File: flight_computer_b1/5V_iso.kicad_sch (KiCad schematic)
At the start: 1 part, among them U7 MIC94161YCS-TR

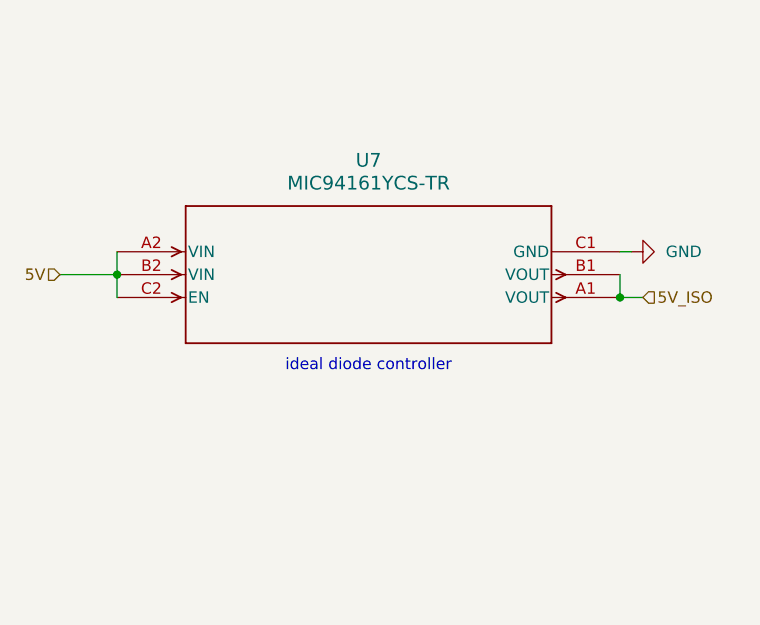
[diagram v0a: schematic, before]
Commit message: flight computer: added mux and voltage sense channels
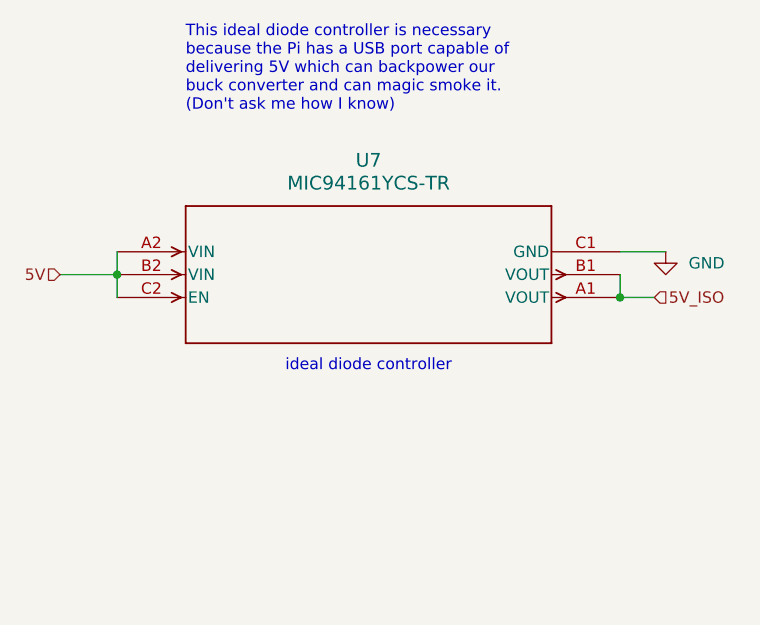
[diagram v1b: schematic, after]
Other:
- note added: "This ideal diode controller is necessary because the Pi has a USB port capable of delivering 5V which can backpower our buck converter and can magic smoke it. (Don't ask me how I know)"
- company: (none) -> Purdue Space Program Liquids
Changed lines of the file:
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@@
 	(generator_version "9.0")
 	(paper "A4")
+	(title_block
+		(date "2025-11-05")
+		(rev "1")
+		(company "Purdue Space Program Liquids")
+	)
 	(text "ideal diode controller"
 		(exclude_from_sim no)
@@
 				(size 1.27 1.27)
 			)
+		)
+	)
+	(text "This ideal diode controller is necessary\nbecause the Pi has a USB port capable of\ndelivering 5V which can backpower our\nbuck converter and can magic smoke it.\n(Don't ask me how I know)"
+		(exclude_from_sim no)
+		(at 114.3 69.85 0)
+		(effects
+			(font
+				(size 1.27 1.27)
+			)
+			(justify left)
 		)
 	)
@@
 	(wire
 		(pts
-			(xy 162.56 95.25) (xy 165.1 95.25)
+			(xy 162.56 95.25) (xy 166.37 95.25)
 		)
 		(stroke
@@
 	(wire
 		(pts
-			(xy 163.83 90.17) (xy 162.56 90.17)
+			(xy 167.64 90.17) (xy 162.56 90.17)
 		)
 		(stroke
@@
 	(hierarchical_label "5V_ISO"
 		(shape input)
-		(at 165.1 95.25 0)
+		(at 166.37 95.25 0)
 		(effects
 			(font
@@
 	(symbol
 		(lib_id "power:GND")
-		(at 163.83 90.17 90)
+		(at 167.64 90.17 0)
 		(unit 1)
 		(exclude_from_sim no)
@@
 		(fields_autoplaced yes)
 		(property "Reference" "#PWR055"
-			(at 170.18 90.17 0)
+			(at 167.64 96.52 0)
 			(effects
 				(font
@@
 		)
 		(property "Value" "GND"
-			(at 167.64 90.1699 90)
+			(at 170.18 91.4399 0)
 			(effects
 				(font
 					(size 1.27 1.27)
 				)
-				(justify right)
+				(justify left)
 			)
 		)
 		(property "Footprint" ""
-			(at 163.83 90.17 0)
+			(at 167.64 90.17 0)
 			(effects
 				(font
@@
 		)
 		(property "Datasheet" ""
-			(at 163.83 90.17 0)
+			(at 167.64 90.17 0)
 			(effects
 				(font
@@
 		)
 		(property "Description" "Power symbol creates a global label with name \"GND\" , ground"
-			(at 163.83 90.17 0)
+			(at 167.64 90.17 0)
 			(effects
 				(font

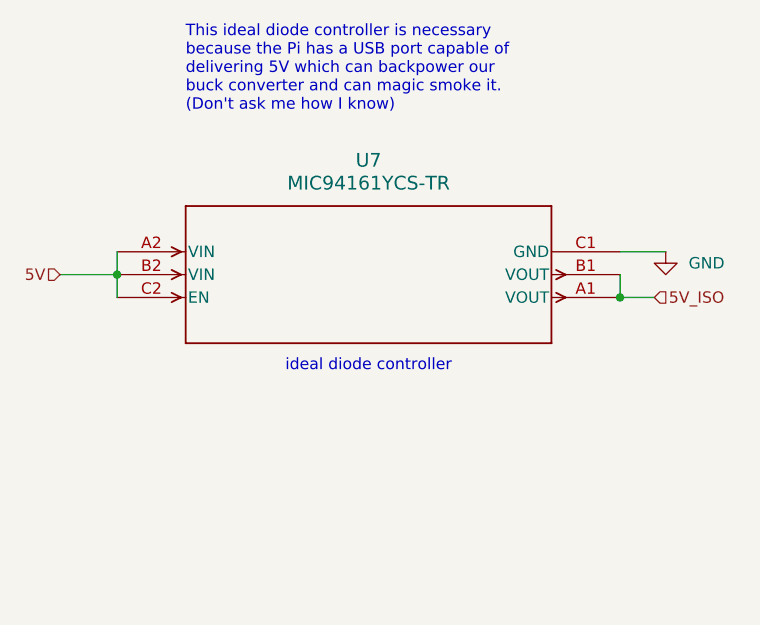
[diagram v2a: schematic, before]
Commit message: flight computer: new ideal diode, small schematic changes
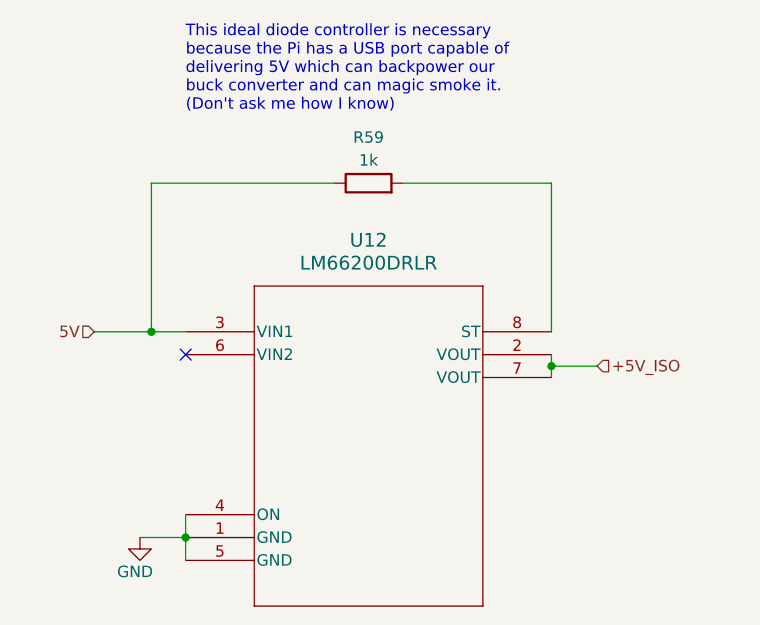
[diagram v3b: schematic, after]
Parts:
- removed U7: MIC94161YCS-TR, avi_lib:MIC94161YCS_TR, symbol avi_lib:MIC94161YCS-TR
- added R59: 1k, Resistor_SMD:R_0603_1608Metric, symbol Device:R
- added U12: LM66200DRLR, avi_lib:SOT-5X3_DRL_TEX-L, symbol avi_lib:LM66200DRLR
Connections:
- net 5V: now also R59.1, U12.3 (VIN1)
- net GND: now also U12.1 (GND), U12.4 (ON), U12.5 (GND)
- new net: R59.2, U12.8 (ST)
- new net +5V_ISO: U12.2 (VOUT), U12.7 (VOUT)
- no-connect marks 0 -> 1
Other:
- note removed: "ideal diode controller"

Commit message: flight computer: routing updates
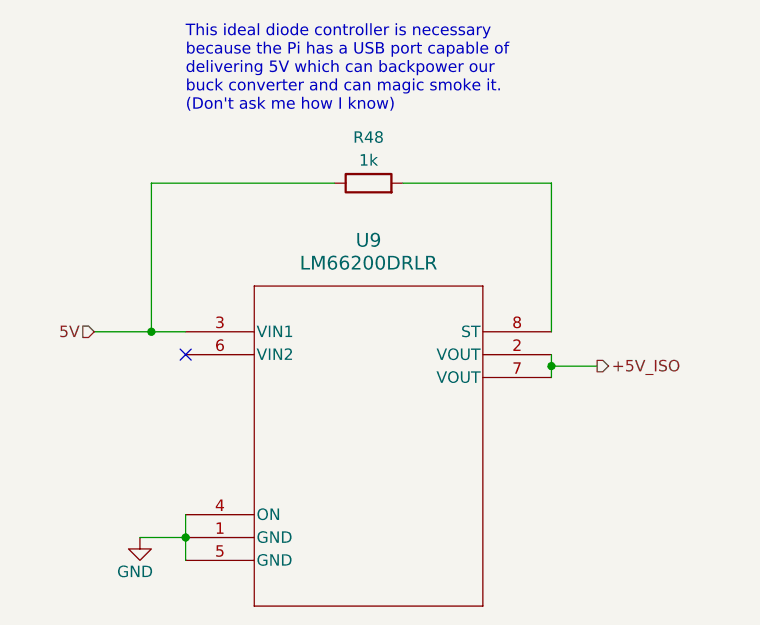
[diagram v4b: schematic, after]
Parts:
- renumbered R59 to R48, U12 to U9
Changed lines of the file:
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@@
 	)
 	(hierarchical_label "+5V_ISO"
-		(shape input)
+		(shape output)
 		(at 160.02 102.87 0)
 		(effects
@@
 		(on_board yes)
 		(dnp no)
-		(property "Reference" "#PWR055"
+		(property "Reference" "#PWR062"
 			(at 109.22 128.27 0)
 			(effects
@@
 			(project "flight_computer"
 				(path "/b71a7b79-cdb5-4e38-a72c-0daaa3474f05/4c75cebc-ee68-4292-a47b-c723457cf341"
-					(reference "#PWR055")
+					(reference "#PWR062")
 					(unit 1)
 				)
@@
 		(on_board yes)
 		(dnp no)
-		(property "Reference" "R59"
+		(property "Reference" "R48"
 			(at 134.62 77.47 90)
 			(effects
@@
 			(project "flight_computer"
 				(path "/b71a7b79-cdb5-4e38-a72c-0daaa3474f05/4c75cebc-ee68-4292-a47b-c723457cf341"
-					(reference "R59")
+					(reference "R48")
 					(unit 1)
 				)
@@
 		(dnp no)
 		(fields_autoplaced yes)
-		(property "Reference" "U12"
+		(property "Reference" "U9"
 			(at 134.62 88.9 0)
 			(effects
@@
 			(project ""
 				(path "/b71a7b79-cdb5-4e38-a72c-0daaa3474f05/4c75cebc-ee68-4292-a47b-c723457cf341"
-					(reference "U12")
+					(reference "U9")
 					(unit 1)
 				)

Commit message: flight computer: new pyro circuit
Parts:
- U9: DIGIKEY PART N (none) -> 296-LM66200DRLRCT-ND
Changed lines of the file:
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@@
+			)
+		)
+		(property "DIGIKEY PART N" "296-LM66200DRLRCT-ND"
+			(at 114.3 99.06 0)
+			(effects
+				(font
+					(size 1.27 1.27)
+				)
+				(hide yes)
 			)
 		)
